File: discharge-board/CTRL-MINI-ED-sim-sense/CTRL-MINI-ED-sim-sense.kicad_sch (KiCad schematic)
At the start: 23 parts, among them U1 Opamp_Dual

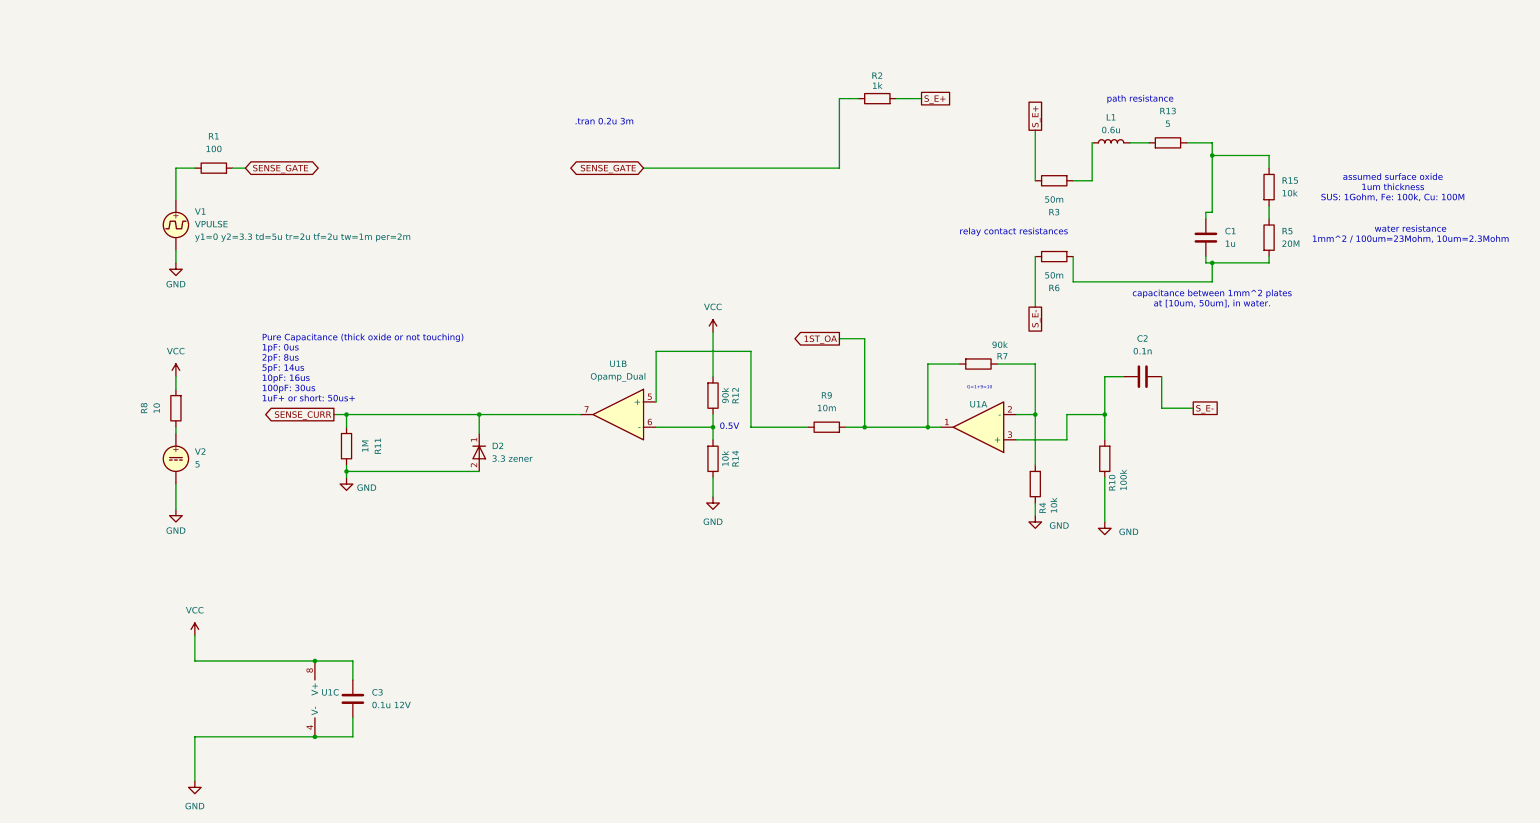
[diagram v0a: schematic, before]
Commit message: CTRL-MINI-ED r1 draft schematics
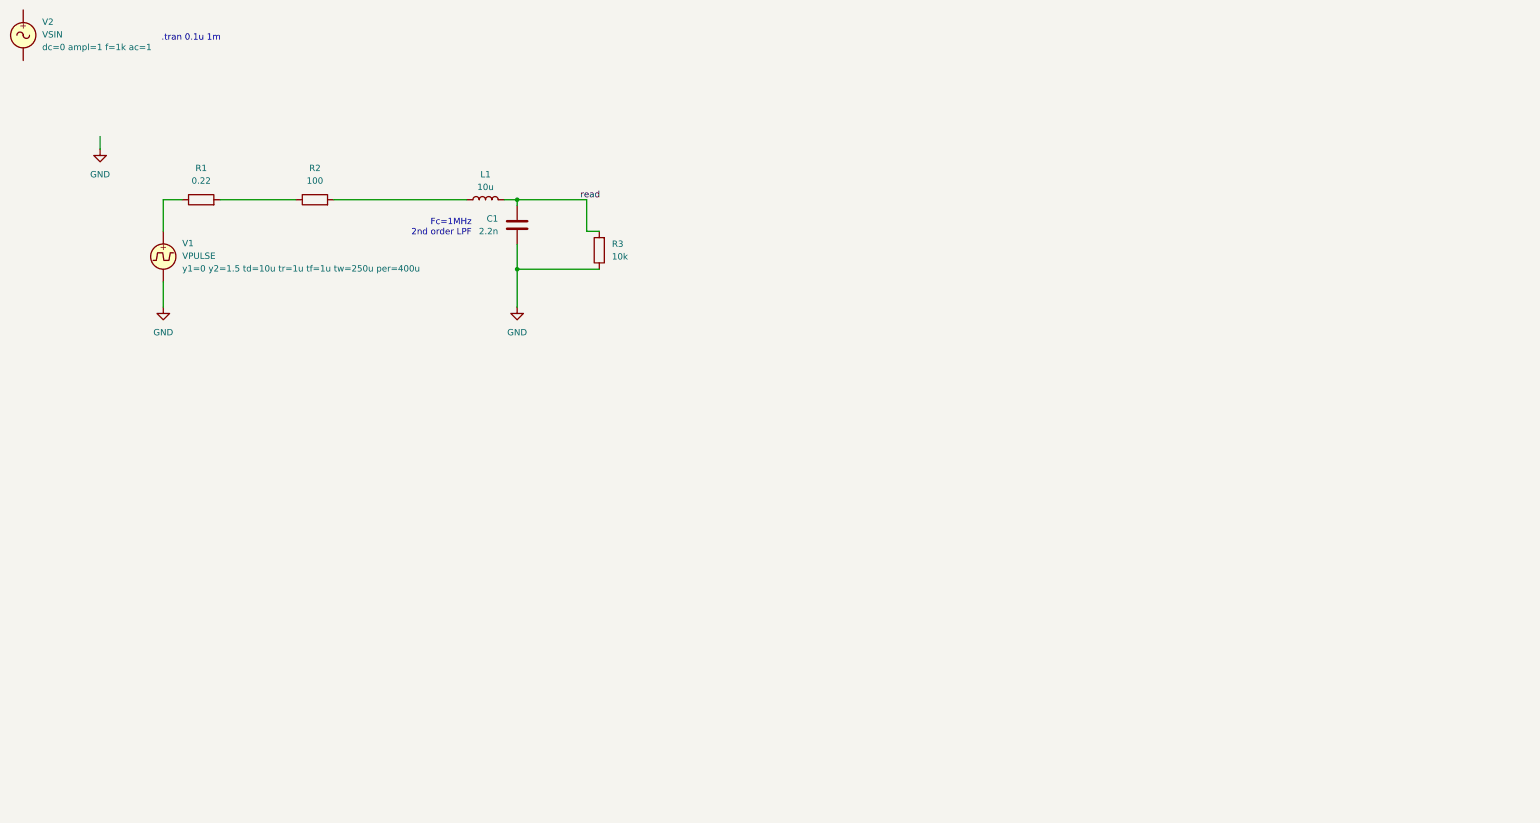
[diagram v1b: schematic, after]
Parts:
- removed C2: 0.1n, symbol Device:C
- removed C3: 0.1u 12V, Capacitor_SMD:C_0603_1608Metric, symbol Device:C
- removed D2: 3.3 zener, symbol Simulation_SPICE:D
- removed R10: 100k, Resistor_SMD:R_0603_1608Metric, symbol Device:R
- removed R11: 1M, symbol Device:R
- removed R12, R7: 90k, Resistor_SMD:R_0603_1608Metric, symbol Device:R
- removed R13: 5, symbol Device:R
- removed R14, R4: 10k, Resistor_SMD:R_0603_1608Metric, symbol Device:R
- removed R15: 10k, symbol Device:R
- removed R5: 20M, symbol Device:R
- removed R6: 50m, symbol Device:R
- removed R8: 10, Resistor_SMD:R_0603_1608Metric, symbol Device:R
- removed R9: 10m, Resistor_SMD:R_0603_1608Metric, symbol Device:R
- removed U1: Opamp_Dual, symbol Device:Opamp_Dual
- removed V2: 5, symbol Simulation_SPICE:VDC
- added V2: VSIN, symbol Simulation_SPICE:VSIN
- C1: value 1u -> 2.2n
- L1: value 0.6u -> 10u
- R1: value 100 -> 0.22; footprint Resistor_SMD:R_0603_1608Metric -> (none)
- R2: value 1k -> 100; footprint Resistor_SMD:R_0603_1608Metric -> (none)
- R3: value 50m -> 10k
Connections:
- net GND: now also C1.2, R3.1
- net read: now reaches C1.1
- net read: now also L1.2, R3.2
- net at L1.1: now also R2.2; no longer R3.2
- net SENSE_GATE: no longer names the net of R1.2, R2.1
- removed net S_E+: R2.2, R3.1
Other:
- note added: ".tran 0.1u 1m"
- note added: "Fc=1MHz 2nd order LPF"
- note removed: ".tran 0.2u 3m"
- note removed: "0.5V"
- note removed: "G=1+9=10"
- note removed: "Pure Capacitance (thick oxide or not touching) 1pF: 0us 2pF: 8us 5pF: 14us 10pF: 16us 100pF: 30us 1uF+ or short: 50us+"
- note removed: "assumed surface oxide 1um thickness SUS: 1Gohm, Fe: 100k, Cu: 100M"
- note removed: "capacitance between 1mm^2 plates at [10um, 50um], in water."
- note removed: "path resistance"
- note removed: "relay contact resistances"
- note removed: "water resistance 1mm^2 / 100um=23Mohm, 10um=2.3Mohm"

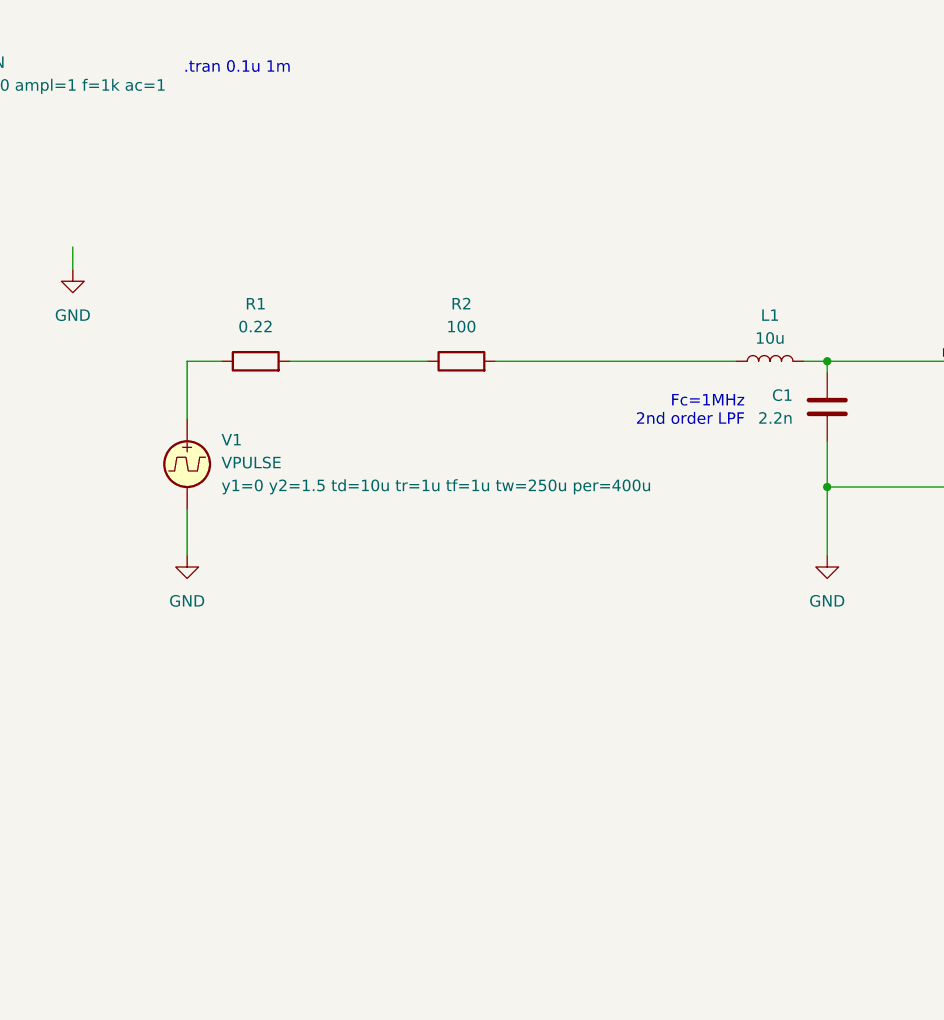
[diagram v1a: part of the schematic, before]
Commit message: Add PWM voltage divider and refactor
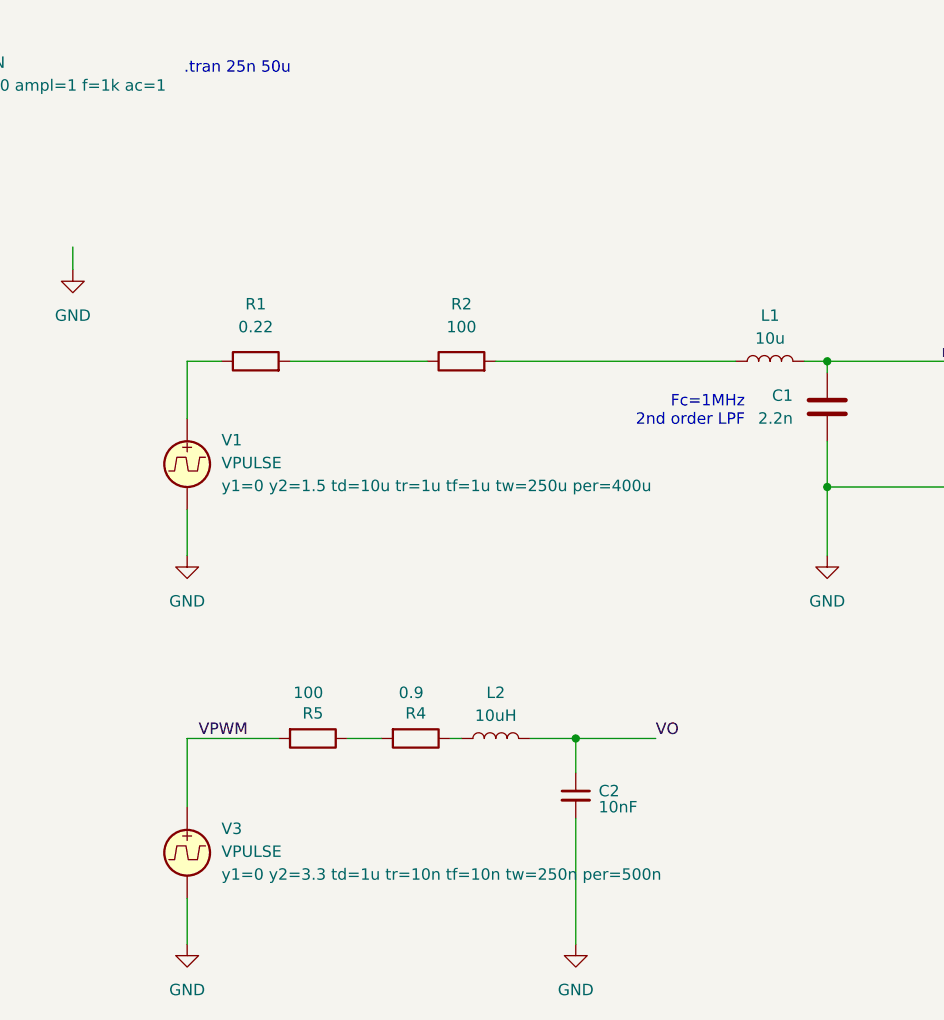
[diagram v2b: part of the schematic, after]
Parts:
- added C2: 10nF, Capacitor_SMD:C_0603_1608Metric, symbol Device:C_Small
- added L2: 10uH, Inductor_SMD:L_0603_1608Metric, symbol Device:L
- added R4: 0.9, Resistor_SMD:R_0603_1608Metric, symbol Device:R
- added R5: 100, Resistor_SMD:R_0603_1608Metric, symbol Device:R
- added V3: VPULSE, symbol Simulation_SPICE:VPULSE
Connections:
- net GND: now also C2.2, V3.2
- new net: L2.1, R4.1
- new net: R4.2, R5.1
- new net VO: C2.1, L2.2
- new net VPWM: R5.2, V3.1
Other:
- note added: ".tran 25n 50u"
- note removed: ".tran 0.1u 1m"

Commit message: Add netlist class
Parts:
- added R6: 470, Resistor_SMD:R_0603_1608Metric, symbol Device:R
- L2: value 10uH -> 10u
- R5: value 100 -> 470
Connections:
- net GND: now also R6.2
- net at R4.2, R5.1: now also R6.1
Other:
- moved on the sheet: R5
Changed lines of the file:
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@@
 	(paper "A4")
+	(junction
+		(at 55.88 120.65)
+		(diameter 0)
+		(color 0 0 0 0)
+	)
 	(junction
 		(at 99.06 100.33)
@@
 	)
 	(junction
+		(at 76.2 100.33)
+		(diameter 0)
+		(color 0 0 0 0)
+	)
+	(junction
 		(at 127 58.42)
 		(diameter 0)
@@
 	(wire
 		(pts
-			(xy 55.88 118.11) (xy 55.88 123.19)
+			(xy 76.2 111.76) (xy 76.2 120.65)
+		)
+		(stroke
+			(width 0)
+			(type default)
+		)
+	)
+	(wire
+		(pts
+			(xy 55.88 118.11) (xy 55.88 120.65)
+		)
+		(stroke
+			(width 0)
+			(type default)
+		)
+	)
+	(wire
+		(pts
+			(xy 76.2 120.65) (xy 55.88 120.65)
 		)
 		(stroke
@@
 	(wire
 		(pts
+			(xy 76.2 100.33) (xy 76.2 104.14)
+		)
+		(stroke
+			(width 0)
+			(type default)
+		)
+	)
+	(wire
+		(pts
 			(xy 59.69 58.42) (xy 55.88 58.42)
 		)
@@
 	(wire
 		(pts
-			(xy 73.66 100.33) (xy 77.47 100.33)
+			(xy 72.39 100.33) (xy 76.2 100.33)
 		)
 		(stroke
@@
 	(wire
 		(pts
-			(xy 55.88 100.33) (xy 66.04 100.33)
+			(xy 55.88 100.33) (xy 64.77 100.33)
 		)
 		(stroke
@@
 	(wire
 		(pts
+			(xy 55.88 120.65) (xy 55.88 123.19)
+		)
+		(stroke
+			(width 0)
+			(type default)
+		)
+	)
+	(wire
+		(pts
 			(xy 140.97 64.77) (xy 143.51 64.77)
 		)
@@
 		(pts
 			(xy 127 67.31) (xy 127 72.39)
+		)
+		(stroke
+			(width 0)
+			(type default)
+		)
+	)
+	(wire
+		(pts
+			(xy 76.2 100.33) (xy 77.47 100.33)
 		)
 		(stroke
@@
 			)
 		)
-		(property "Value" "10uH"
+		(property "Value" "10u"
 			(at 90.17 97.79 90)
 			(effects
@@
 			)
 		)
-		(property "Sim.Library" ""
-			(at 90.17 100.33 0)
-			(effects
-				(font
-					(size 1.27 1.27)
-				)
-				(hide yes)
-			)
-		)
-		(property "Sim.Name" ""
-			(at 90.17 100.33 0)
-			(effects
-				(font
-					(size 1.27 1.27)
-				)
-				(hide yes)
-			)
-		)
-		(property "Sim.Type" ""
-			(at 90.17 100.33 0)
-			(effects
-				(font
-					(size 1.27 1.27)
-				)
-				(hide yes)
-			)
-		)
 		(property "LCSC" "C86083"
 			(at 90.17 100.33 90)
@@
 			)
 		)
-		(property "Sim.Params" "IND=10e-6 CSECT=6.4e-8 DIA=0.8e-3 LENGTH=1.6e-3 TC1=0.001 TC2=0.0001 TNOM=25 MU=100"
-			(at 90.17 100.33 90)
+		(property "Sim.Device" "L"
+			(at 90.17 100.33 0)
+			(effects
+				(font
+					(size 1.27 1.27)
+				)
+				(hide yes)
+			)
+		)
+		(property "Sim.Pins" "1=+ 2=-"
+			(at 90.17 100.33 0)
 			(effects
 				(font
@@
 	)
 	(symbol
+		(lib_id "Device:R")
+		(at 76.2 107.95 0)
+		(unit 1)
+		(exclude_from_sim no)
+		(in_bom yes)
+		(on_board yes)
+		(dnp no)
+		(property "Reference" "R6"
+			(at 73.406 107.95 90)
+			(effects
+				(font
+					(size 1.27 1.27)
+				)
+			)
+		)
+		(property "Value" "470"
+			(at 71.12 108.458 90)
+			(effects
+				(font
+					(size 1.27 1.27)
+				)
+			)
+		)
+		(property "Footprint" "Resistor_SMD:R_0603_1608Metric"
+			(at 74.422 107.95 90)
+			(effects
+				(font
+					(size 1.27 1.27)
+				)
+				(hide yes)
+			)
+		)
+		(property "Datasheet" "~"
+			(at 76.2 107.95 0)
+			(effects
+				(font
+					(size 1.27 1.27)
+				)
+				(hide yes)
+			)
+		)
+		(property "Description" "Resistor"
+			(at 76.2 107.95 0)
+			(effects
+				(font
+					(size 1.27 1.27)
+				)
+				(hide yes)
+			)
+		)
+		(property "LCSC" "C21190"
+			(at 76.2 107.95 0)
+			(effects
+				(font
+					(size 1.27 1.27)
+				)
+				(hide yes)
+			)
+		)
+		(property "Sim.Library" ""
+			(at 76.2 107.95 0)
+			(effects
+				(font
+					(size 1.27 1.27)
+				)
+				(hide yes)
+			)
+		)
+		(property "Sim.Name" ""
+			(at 76.2 107.95 0)
+			(effects
+				(font
+					(size 1.27 1.27)
+				)
+				(hide yes)
+			)
+		)
+		(property "Sim.Type" ""
+			(at 76.2 107.95 0)
+			(effects
+				(font
+					(size 1.27 1.27)
+				)
+				(hide yes)
+			)
+		)
+		(pin "1"
+		)
+		(pin "2"
+		)
+		(instances
+			(project "CTRL-MINI-ED-sim-sense"
+				(path "/3fa1ca74-4d0d-40dd-8b5c-0d4be11bd5b5"
+					(reference "R6")
+					(unit 1)
+				)
+			)
+		)
+	)
+	(symbol
 		(lib_id "power:GND")
 		(at 55.88 80.01 0)
@@
 	(symbol
 		(lib_id "Device:R")
-		(at 69.85 100.33 270)
+		(at 68.58 100.33 270)
 		(unit 1)
 		(exclude_from_sim no)
@@
 		(dnp no)
 		(property "Reference" "R5"
-			(at 69.85 97.536 90)
-			(effects
-				(font
-					(size 1.27 1.27)
-				)
-			)
-		)
-		(property "Value" "100"
-			(at 69.342 95.25 90)
+			(at 68.58 97.536 90)
+			(effects
+				(font
+					(size 1.27 1.27)
+				)
+			)
+		)
+		(property "Value" "470"
+			(at 68.072 95.25 90)
 			(effects
 				(font
@@
 		)
 		(property "Footprint" "Resistor_SMD:R_0603_1608Metric"
-			(at 69.85 98.552 90)
+			(at 68.58 98.552 90)
 			(effects
 				(font
@@
 		)
 		(property "Datasheet" "~"
-			(at 69.85 100.33 0)
+			(at 68.58 100.33 0)
 			(effects
 				(font
@@
 		)
 		(property "Description" "Resistor"
-			(at 69.85 100.33 0)
+			(at 68.58 100.33 0)
 			(effects
 				(font
@@
 		)
 		(property "LCSC" "C21190"
-			(at 69.85 100.33 0)
+			(at 68.58 100.33 0)
 			(effects
 				(font
@@
 		)
 		(property "Sim.Library" ""
-			(at 69.85 100.33 0)
+			(at 68.58 100.33 0)
 			(effects
 				(font
@@
 		)
 		(property "Sim.Name" ""
-			(at 69.85 100.33 0)
+			(at 68.58 100.33 0)
 			(effects
 				(font
@@
 		)
 		(property "Sim.Type" ""
-			(at 69.85 100.33 0)
-			(effects
-				(font
+			(at 68.58 100.33 0)
+			(effects
+				(font
